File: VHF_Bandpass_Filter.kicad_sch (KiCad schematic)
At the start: 20 parts

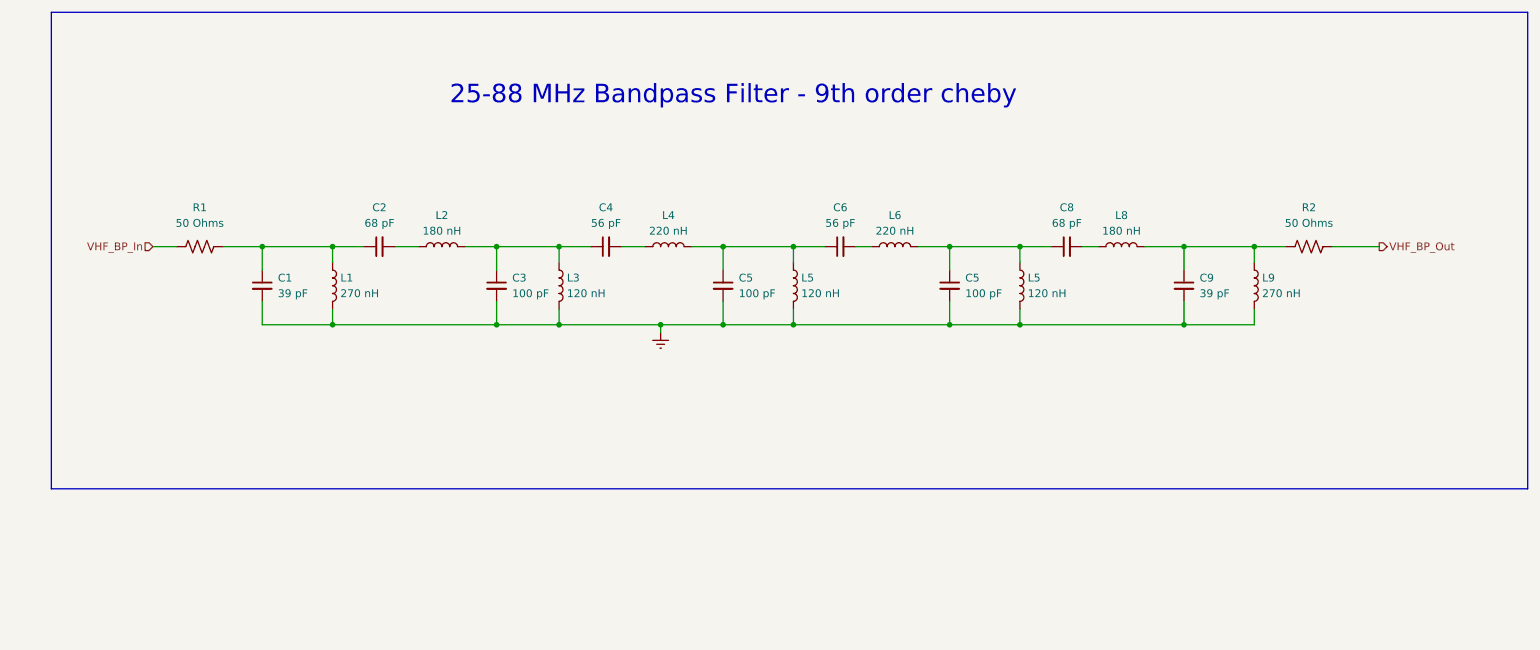
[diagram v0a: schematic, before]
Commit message: Redefined filters & Top Level Diagram
- Implement wider filters to accomodate 10% tolerance parts.
- Break design in to top-level heirarchical blocks.
- Start wiring some of the blocks together.
- Add L-Band segment, but is currently just a copy of the UHF filter.
- Add the start of a TX path.
- Add placeholders for power and band/tune control.
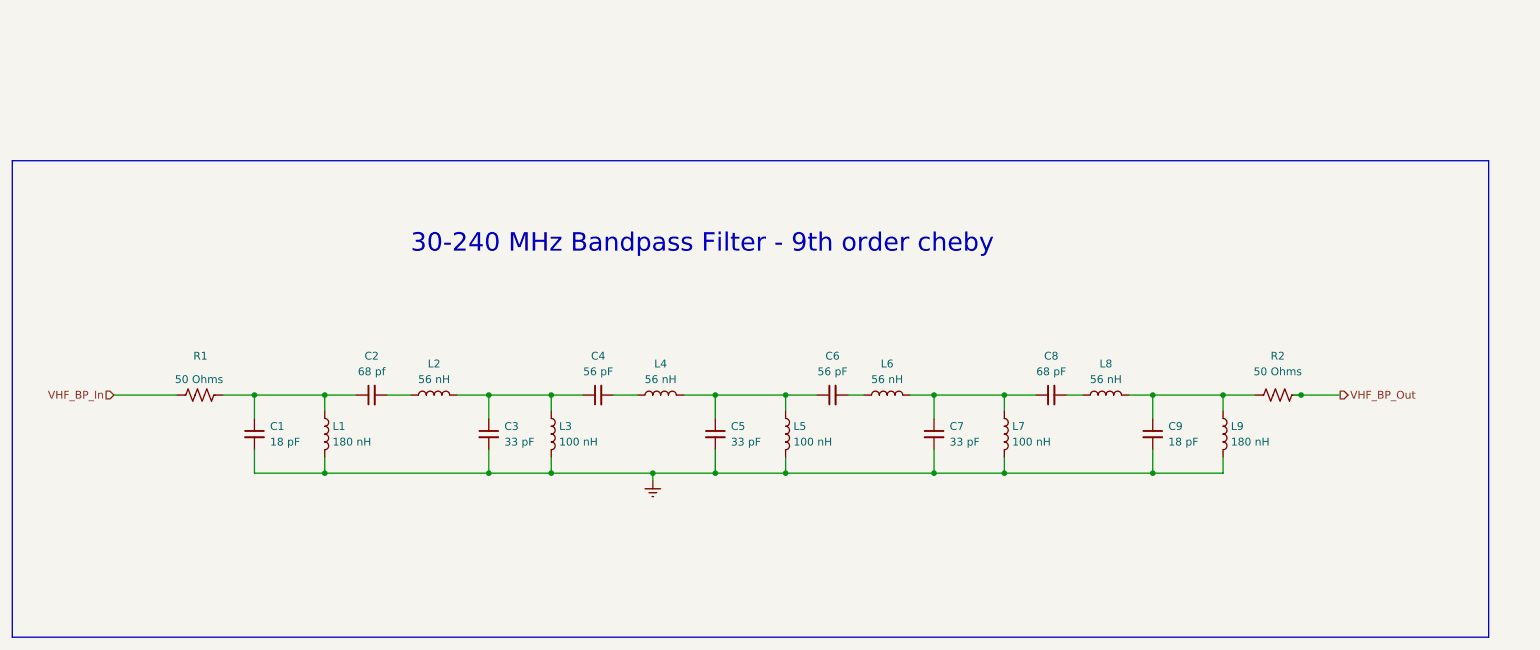
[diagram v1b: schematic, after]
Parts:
- removed C5 (x2): 100 pF, symbol Device:C_Small
- removed L5 (x2): 120 nH, symbol Device:L
- added C5, C7: 33 pF, Capacitor_SMD:C_1206_3216Metric, symbol Device:C_Small
- added L5, L7: 100 nH, Inductor_SMD:L_1206_3216Metric, symbol Device:L
- C1, C9: value 39 pF -> 18 pF; footprint (none) -> Capacitor_SMD:C_1206_3216Metric
- C2: value 68 pF -> 68 pf; footprint (none) -> Capacitor_SMD:C_1206_3216Metric
- C3: value 100 pF -> 33 pF; footprint (none) -> Capacitor_SMD:C_1206_3216Metric
- C4, C6, C8: footprint (none) -> Capacitor_SMD:C_1206_3216Metric
- L1, L9: value 270 nH -> 180 nH; footprint (none) -> Inductor_SMD:L_1206_3216Metric
- L2, L8: value 180 nH -> 56 nH; footprint (none) -> Inductor_SMD:L_1206_3216Metric
- L3: value 120 nH -> 100 nH; footprint (none) -> Inductor_SMD:L_1206_3216Metric
- L4, L6: value 220 nH -> 56 nH; footprint (none) -> Inductor_SMD:L_1206_3216Metric
- R1, R2: footprint (none) -> Resistor_SMD:R_1206_3216Metric
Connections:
- net Earth: now also C5.2, C7.2, L5.2, L7.2
- net at C6.1, L4.2: now also C5.1, L5.1
- net at C8.1, L6.2: now also C7.1, L7.1
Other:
- note added: "30-240 MHz Bandpass Filter - 9th order cheby"
- note removed: "25-88 MHz Bandpass Filter - 9th order cheby"

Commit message: More filter work. Add project title to drawings.
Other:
- company: (none) -> Steves Custom Computers
- title: (none) -> PLUTO RF Card Front-End
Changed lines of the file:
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@@
 (kicad_sch (version 20230121) (generator eeschema)
   (paper "A4")
+  (title_block
+    (title "PLUTO RF Card Front-End")
+    (rev " 001")
+    (company "Steves Custom Computers")
+  )
   (junction (at 100.33 121.92) (diameter 0) (color 0 0 0 0)
   )

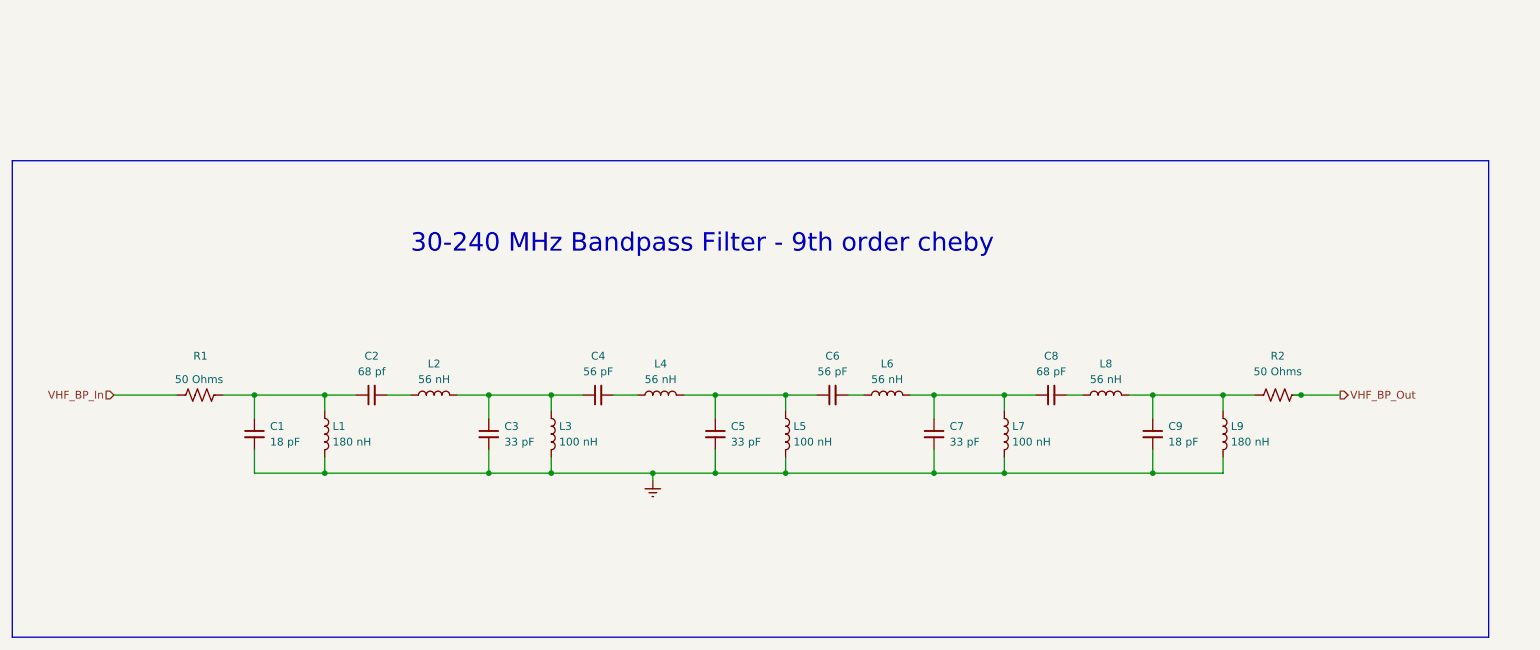
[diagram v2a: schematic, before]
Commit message: Major restructure. Add power/control busses.
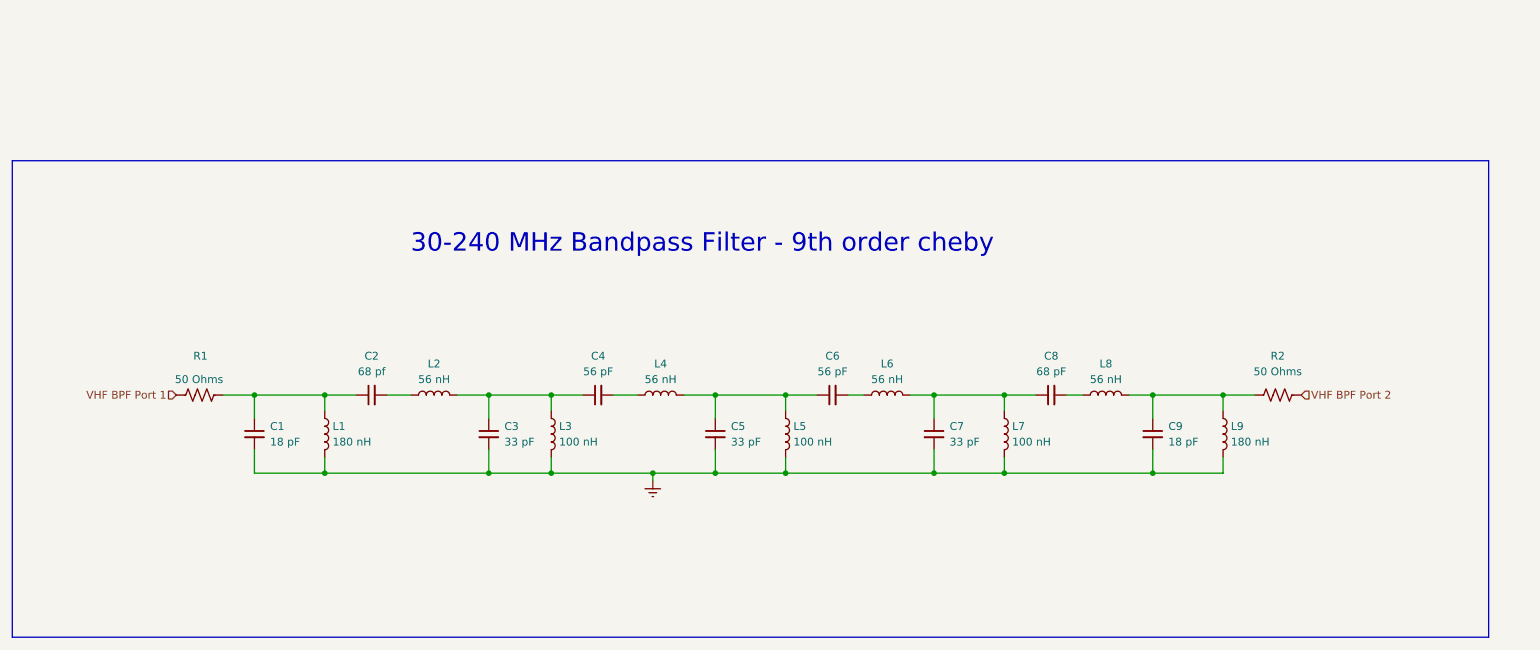
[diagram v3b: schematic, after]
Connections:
- net VHF_BP_In renamed VHF BPF Port 1
- net VHF_BP_Out renamed VHF BPF Port 2
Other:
- title: PLUTO RF Card Front-End -> PLUTO RF Front-End Card
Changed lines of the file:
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@@
   (paper "A4")
   (title_block
-    (title "PLUTO RF Card Front-End")
+    (title "PLUTO RF Front-End Card")
     (rev " 001")
     (company "Steves Custom Computers")
@@
   (junction (at 184.15 109.22) (diameter 0) (color 0 0 0 0)
   )
-  (junction (at 232.41 109.22) (diameter 0) (color 0 0 0 0)
-  )
   (junction (at 137.16 109.22) (diameter 0) (color 0 0 0 0)
   )
@@
     (stroke (width 0) (type default))
   )
-  (wire (pts (xy 39.37 109.22) (xy 49.53 109.22))
-    (stroke (width 0) (type default))
-  )
   (wire (pts (xy 208.28 118.11) (xy 208.28 121.92))
     (stroke (width 0) (type default))
@@
     (stroke (width 0) (type default))
   )
-  (wire (pts (xy 231.14 109.22) (xy 232.41 109.22))
-    (stroke (width 0) (type default))
-  )
   (wire (pts (xy 110.49 119.38) (xy 110.49 121.92))
     (stroke (width 0) (type default))
@@
   )
   (wire (pts (xy 148.59 109.22) (xy 137.16 109.22))
-    (stroke (width 0) (type default))
-  )
-  (wire (pts (xy 232.41 109.22) (xy 238.76 109.22))
     (stroke (width 0) (type default))
   )
@@
     (effects (font (size 3 3)) (justify left bottom))
   )
-  (hierarchical_label "VHF_BP_Out" (shape output) (at 238.76 109.22 0) (fields_autoplaced)
+  (hierarchical_label "VHF BPF Port 2" (shape input) (at 232.41 109.22 0) (fields_autoplaced)
     (effects (font (size 1.27 1.27)) (justify left))
   )
-  (hierarchical_label "VHF_BP_In" (shape input) (at 39.37 109.22 180) (fields_autoplaced)
+  (hierarchical_label "VHF BPF Port 1" (shape input) (at 49.53 109.22 180) (fields_autoplaced)
     (effects (font (size 1.27 1.27)) (justify right))
   )
